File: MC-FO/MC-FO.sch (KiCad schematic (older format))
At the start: 12 parts

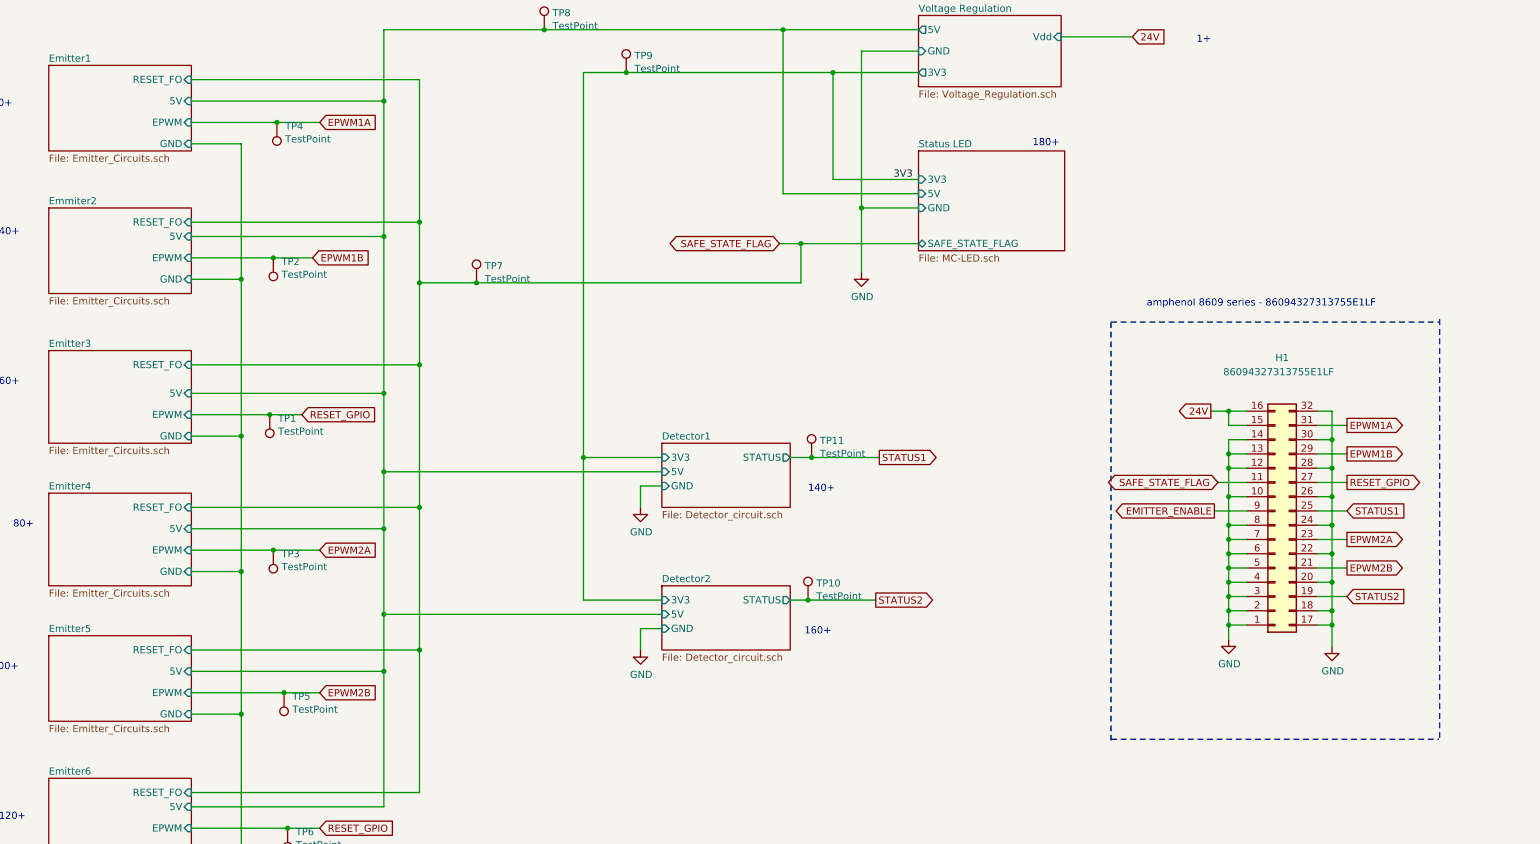
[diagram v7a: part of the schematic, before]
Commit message: updating SAFE_STATE_FLAG and EMITTER_ENABLE
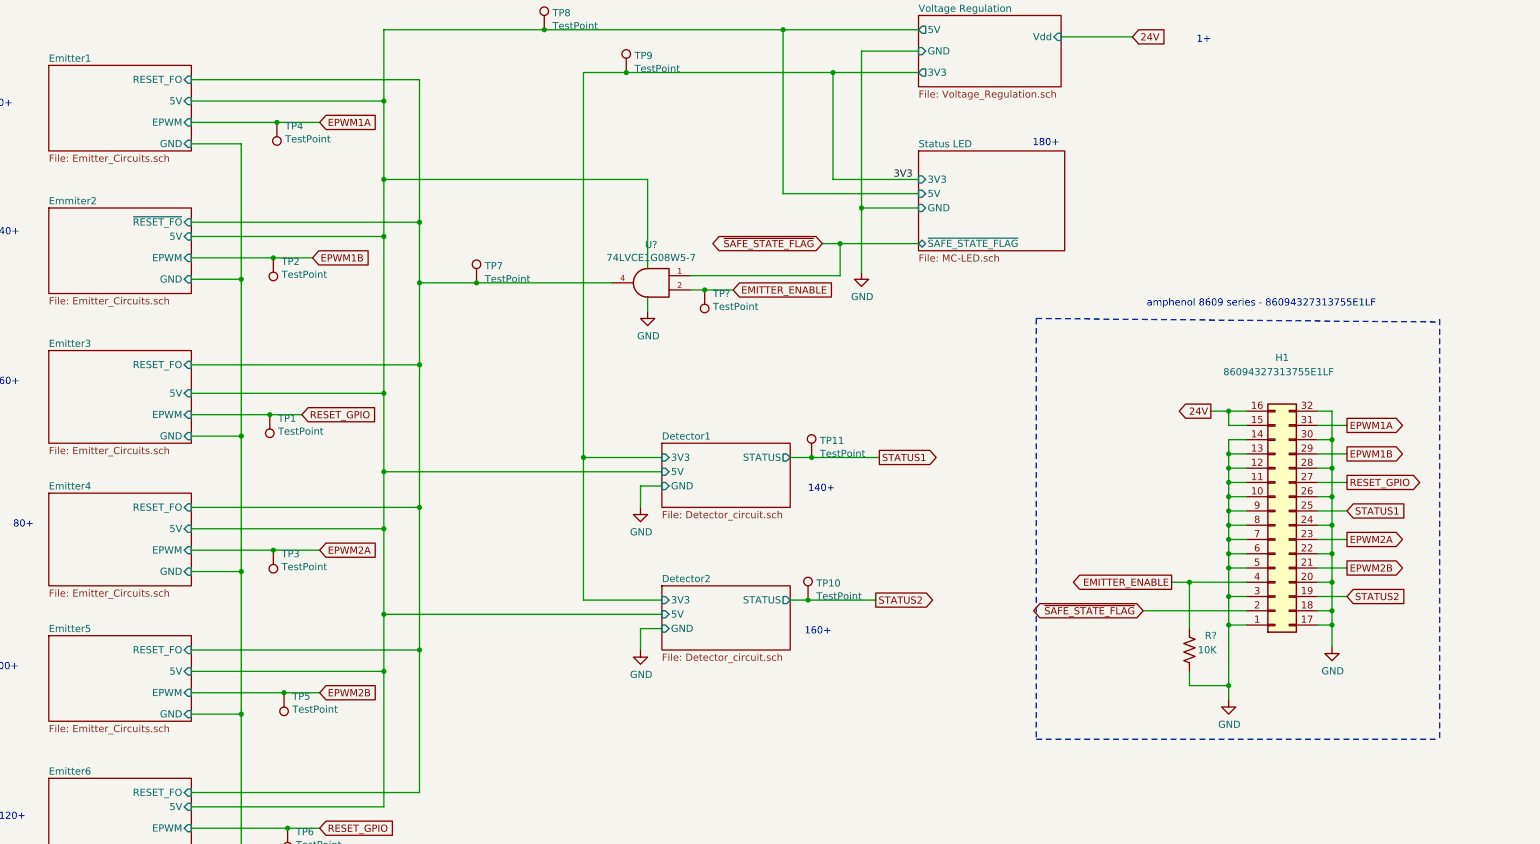
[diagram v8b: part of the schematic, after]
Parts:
- added R?: 10K, Resistor_SMD:R_0603_1608Metric, symbol Device:R_US
- added TP?: TestPoint, TestPoint:TestPoint_Pad_D2.0mm, symbol Connector:TestPoint
- added U?: 74LVCE1G08W5-7, symbol MC-FO:74LVCE1G08W5-7
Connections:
- net EMITTER_ENABLE: now also H1.4 (Pin_4), R?.2, TP?.1, U?.2; no longer H1.9 (Pin_9)
- net GND: now also H1.11 (Pin_11), H1.9 (Pin_9), R?.1, U?.3 (GND); no longer H1.2 (Pin_2), H1.4 (Pin_4)
- net Detector1/5V renamed VCC
- net VCC: now also U?.5 (VCC)
- net SAFE_STATE_FLAG renamed Emitter1/RESET_FO
- net Emitter1/RESET_FO: now also U?.4; no longer H1.11 (Pin_11)
- new net ~SAFE_STATE_FLAG~: H1.2 (Pin_2), U?.1
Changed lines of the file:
@@
 F3 "5V" I R 2050 2300 50
 F4 "GND" I R 2050 2600 50
-F5 "RESET_FO" I R 2050 2200 50
+F5 "~RESET_FO~" I R 2050 2200 50
 $EndSheet
 $Sheet
@@
 F3 "GND" I L 7150 2100 50
 F4 "5V" I L 7150 2000 50
-F5 "SAFE_STATE_FLAG" B L 7150 2350 50
+F5 "~SAFE_STATE_FLAG~" B L 7150 2350 50
 $EndSheet
 Wire Wire Line
@@
 Connection ~ 3400 1350
 Wire Wire Line
-	3400 1350 3400 2300
+	3400 1350 3400 1900
 Wire Wire Line
 	3400 850  3400 1350
@@
 	6550 1900 7150 1900
 Wire Notes Line
-	8500 2900 8500 5850
+	7975 2875 7975 5825
 Wire Notes Line
-	8500 5825 10800 5825
+	7975 5825 10800 5825
 Text Label 6975 1900 0    50   ~ 0
 3V3
@@
 Wire Wire Line
 	6850 4850 6375 4850
-Text GLabel 9250 4025 0    50   BiDi ~ 0
-SAFE_STATE_FLAG
+Text GLabel 8725 4925 0    50   BiDi ~ 0
+~SAFE_STATE_FLAG~
 Wire Wire Line
 	9950 4825 10155 4825
@@
 L power:GND #PWR013
 U 1 1 618DD9E5
-P 9325 5125
-F 0 "#PWR013" H 9325 4875 50  0001 C CNN
-F 1 "GND" H 9330 4952 50  0000 C CNN
-F 2 "" H 9325 5125 50  0001 C CNN
-F 3 "" H 9325 5125 50  0001 C CNN
-	1    9325 5125
+P 9325 5550
+F 0 "#PWR013" H 9325 5300 50  0001 C CNN
+F 1 "GND" H 9330 5377 50  0000 C CNN
+F 2 "" H 9325 5550 50  0001 C CNN
+F 3 "" H 9325 5550 50  0001 C CNN
+	1    9325 5550
 	1    0    0    -1
 $EndComp
 Wire Notes Line
-	8500 2900 10800 2900
-Text GLabel 9225 4225 0    50   Output ~ 0
+	7975 2875 10800 2900
+Text GLabel 8925 4725 0    50   Output ~ 0
 EMITTER_ENABLE
 Wire Wire Line
-	9450 4025 9250 4025
-Wire Wire Line
-	9450 4225 9225 4225
-Text GLabel 6175 2350 0    50   BiDi ~ 0
-SAFE_STATE_FLAG
-Wire Wire Line
-	6175 2350 6325 2350
-Wire Wire Line
-	6325 2350 6325 2625
-Wire Wire Line
-	6325 2625 4050 2625
-Connection ~ 6325 2350
-Wire Wire Line
-	6325 2350 7150 2350
+	9450 4025 9325 4025
+Wire Wire Line
+	9450 4225 9325 4225
+Text GLabel 6475 2350 0    50   BiDi ~ 0
+~SAFE_STATE_FLAG~
+Wire Wire Line
+	6475 2350 6600 2350
+Wire Wire Line
+	6600 2350 6600 2575
+Connection ~ 6600 2350
+Wire Wire Line
+	6600 2350 7150 2350
 Connection ~ 3650 2625
 Wire Wire Line
@@
 	9450 4125 9325 4125
 Wire Wire Line
-	9325 3925 9325 4125
+	9325 3925 9325 4025
 Connection ~ 9325 4125
 Wire Wire Line
-	9325 4125 9325 4325
+	9325 4125 9325 4225
 Connection ~ 9325 4325
 Wire Wire Line
@@
 Connection ~ 9325 4625
 Wire Wire Line
-	9325 4625 9325 4725
-Wire Wire Line
-	9450 4725 9325 4725
-Connection ~ 9325 4725
-Wire Wire Line
-	9325 4725 9325 4825
-Wire Wire Line
 	9450 4825 9325 4825
-Connection ~ 9325 4825
-Wire Wire Line
-	9325 4825 9325 4925
-Wire Wire Line
-	9450 4925 9325 4925
-Connection ~ 9325 4925
-Wire Wire Line
-	9325 4925 9325 5025
 Wire Wire Line
 	9450 5025 9325 5025
-Connection ~ 9325 5025
-Wire Wire Line
-	9325 5025 9325 5125
+Wire Wire Line
+	9325 5025 9325 5450
 Wire Wire Line
 	9325 3525 9325 3625
@@
 	1    0    0    -1
 $EndComp
-Connection ~ 4050 2625
 Wire Wire Line
 	4050 2625 3650 2625
@@
 Wire Wire Line
 	2650 1500 2950 1500
+$Comp
+L MC-FO:74LVCE1G08W5-7 U?
+U 1 1 62292B2D
+P 5250 2625
+F 0 "U?" H 5225 2892 50  0000 C CNN
+F 1 "74LVCE1G08W5-7" H 5225 2801 50  0000 C CNN
+F 2 "" H 5250 2625 50  0001 C CNN
+F 3 "https://www.diodes.com/assets/Datasheets/74LVCE1G08.pdf" H 5250 2625 50  0001 C CNN
+	1    5250 2625
+	-1   0    0    -1
+$EndComp
+Wire Wire Line
+	5550 2575 6600 2575
+Wire Wire Line
+	5550 2675 5650 2675
+Wire Wire Line
+	4050 2625 5000 2625
+Connection ~ 4050 2625
+Text GLabel 5850 2675 2    50   Input ~ 0
+EMITTER_ENABLE
+$Comp
+L power:GND #PWR?
+U 1 1 622BADE1
+P 5250 2825
+F 0 "#PWR?" H 5250 2575 50  0001 C CNN
+F 1 "GND" H 5255 2652 50  0000 C CNN
+F 2 "" H 5250 2825 50  0001 C CNN
+F 3 "" H 5250 2825 50  0001 C CNN
+	1    5250 2825
+	1    0    0    -1
+$EndComp
+Wire Wire Line
+	5250 2725 5250 2825
+Wire Wire Line
+	5250 2525 5250 1900
+Wire Wire Line
+	5250 1900 3400 1900
+Connection ~ 3400 1900
+Wire Wire Line
+	3400 1900 3400 2300
+Wire Wire Line
+	9450 4925 8725 4925
+Wire Wire Line
+	9325 4625 9325 4825
+Wire Wire Line
+	8925 4725 9050 4725
+Wire Wire Line
+	9325 4825 9325 5025
+Connection ~ 9325 4825
+Connection ~ 9325 5025
+Connection ~ 9325 4025
+Wire Wire Line
+	9325 4025 9325 4125
+Connection ~ 9325 4225
+Wire Wire Line
+	9325 4225 9325 4325
+$Comp
+L Connector:TestPoint TP?
+U 1 1 6230AE4A
+P 5650 2675
+F 0 "TP?" H 5592 2701 50  0000 R CNN
+F 1 "TestPoint" H 5592 2792 50  0000 R CNN
+F 2 "TestPoint:TestPoint_Pad_D2.0mm" H 5850 2675 50  0001 C CNN
+F 3 "~" H 5850 2675 50  0001 C CNN
+	1    5650 2675
+	-1   0    0    1
+$EndComp
+Connection ~ 5650 2675
+Wire Wire Line
+	5650 2675 5850 2675
+Wire Wire Line
+	9050 4725 9050 5050
+Connection ~ 9050 4725
+Wire Wire Line
+	9050 4725 9450 4725
+$Comp
+L Device:R_US R?
+U 1 1 62336059
+P 9050 5200
+AR Path="/6175812E/62336059" Ref="R?"  Part="1"
+AR Path="/62336059" Ref="R?"  Part="1"
+F 0 "R?" H 8900 5100 50  0000 C CNN
+F 1 "10K" H 8925 5200 50  0000 C CNN
+F 2 "Resistor_SMD:R_0603_1608Metric" V 9090 5190 50  0001 C CNN
+F 3 "~" H 9050 5200 50  0001 C CNN
+	1    9050 5200
+	-1   0    0    1
+$EndComp
+Wire Wire Line
+	9050 5350 9050 5450
+Wire Wire Line
+	9050 5450 9325 5450
+Connection ~ 9325 5450
+Wire Wire Line
+	9325 5450 9325 5550
 $EndSCHEMATC
